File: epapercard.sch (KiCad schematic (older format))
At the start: 43 parts, among them P1 CONN_01X06, P2 A120699CT, Q1 2N7002KW, Q2 BSS84W, Q3 AP2305, Q4 BSS84W, Q5 2N7002KW, Q6 2N7002KW, Q7 2N7002KW, SW1 SW_PUSH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

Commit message: Generated BOM
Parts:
- C2: value 100n -> 0.1u
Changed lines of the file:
@@
 P 3500 5500
 F 0 "C2" H 3525 5600 50  0000 L CNN
-F 1 "100n" H 3525 5400 50  0000 L CNN
+F 1 "0.1u" H 3525 5400 50  0000 L CNN
 F 2 "Capacitors_SMD:C_0805_HandSoldering" H 3538 5350 50  0001 C CNN
 F 3 "" H 3500 5500 50  0000 C CNN

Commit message: Changed fet position
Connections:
- net +3V3: now also Q2.2 (S); no longer Q2.3 (D)
- net at C1.2, Q3.1 (G), R1.1: now also Q2.3 (D); no longer Q2.2 (S)
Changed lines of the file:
@@
 $EndComp
 Wire Wire Line
-	1550 700  1550 1300
+	1550 700  1550 800
+Wire Wire Line
+	1550 800  1550 1300
 Wire Wire Line
 	1550 1300 1700 1300
@@
 	8100 4400 9150 4400
 Wire Wire Line
-	9150 4350 9150 4450
+	9150 4350 9150 4400
+Wire Wire Line
+	9150 4400 9150 4450
 Wire Wire Line
 	9150 4350 9650 4350
@@
 $EndComp
 Wire Wire Line
-	6150 5250 8900 5250
+	6150 5250 6250 5250
+Wire Wire Line
+	6250 5250 8900 5250
 Wire Wire Line
 	8900 4950 9650 4950
@@
 	6250 5450 5800 5450
 Wire Wire Line
-	5800 5450 5800 6000
+	5800 5450 5800 5600
+Wire Wire Line
+	5800 5600 5800 6000
 Wire Wire Line
 	5800 5600 6150 5600
@@
 $EndComp
 Wire Wire Line
-	6350 5900 6350 6050
+	6350 5900 6350 6000
+Wire Wire Line
+	6350 6000 6350 6050
 Wire Wire Line
 	6350 6000 6200 6000
@@
 	9500 5600 8250 5600
 Wire Wire Line
-	9500 5150 9500 5600
+	9500 5150 9500 5250
+Wire Wire Line
+	9500 5250 9500 5600
 Wire Wire Line
 	9500 5250 9650 5250
@@
 F 3 "" H 2300 3000 50  0000 C CNN
 	1    2300 3000
-	1    0    0    -1
+	1    0    0    1
 $EndComp
 $Comp
@@
 $EndComp
 Wire Wire Line
-	1350 3600 1550 3600
+	1350 3600 1450 3600
+Wire Wire Line
+	1450 3600 1550 3600
 Text GLabel 1350 3600 0    60   Input ~ 0
 PANEL_ON
@@
 	2550 3300 2400 3300
 Wire Wire Line
-	2400 3300 2400 3200
+	2400 3300 2400 3250
+Wire Wire Line
+	2400 3250 2400 3200
 $Comp
 L R R1
@@
 	1850 3250 1950 3250
 Wire Wire Line
-	2250 3250 3550 3250
+	2250 3250 2400 3250
+Wire Wire Line
+	2400 3250 3550 3250
 Connection ~ 2400 3250
 $Comp
@@
 	2550 3750 2550 3650
 Wire Wire Line
-	2400 2700 2400 2800
+	2400 2700 2400 2750
+Wire Wire Line
+	2400 2750 2400 2800
 Wire Wire Line
 	3350 2900 2700 2900
@@
 $EndComp
 Wire Wire Line
-	3750 2900 4900 2900
+	3750 2900 4000 2900
+Wire Wire Line
+	4000 2900 4450 2900
+Wire Wire Line
+	4450 2900 4900 2900
 Wire Wire Line
 	4000 2900 4000 2950
@@
 DISCHARGE
 Wire Wire Line
-	5750 4550 6100 4550
+	5750 4550 5900 4550
+Wire Wire Line
+	5900 4550 6100 4550
 Connection ~ 5900 4550
 Wire Wire Line
@@
 	6100 1500 6100 1550
 Wire Wire Line
-	6100 1550 6650 1550
+	6100 1550 6350 1550
+Wire Wire Line
+	6350 1550 6650 1550
 Wire Wire Line
 	6350 1550 6350 1600
@@
 	6100 1200 6100 1150
 Wire Wire Line
-	6100 1150 6650 1150
+	6100 1150 6350 1150
+Wire Wire Line
+	6350 1150 6650 1150
 Wire Wire Line
 	6350 1150 6350 1100

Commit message: Adjusting footprints
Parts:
- Q3: value AP2305 -> BSS84W
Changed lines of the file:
@@
 	4200 900  5450 900
-Wire Wire Line
-	9650 1350 9250 1350
-Wire Wire Line
-	9650 1450 9250 1450
-Wire Wire Line
-	9650 1550 9500 1550
-Wire Wire Line
-	9650 1650 9250 1650
-Wire Wire Line
-	9650 1750 9250 1750
-Wire Wire Line
-	9250 1850 9650 1850
-Wire Wire Line
-	9650 1950 9250 1950
 Wire Wire Line
 	8900 2150 9650 2150
@@
 P 3550 3000
 F 0 "Q3" H 3850 3050 50  0000 R CNN
-F 1 "AP2305" H 4050 2950 50  0000 R CNN
+F 1 "BSS84W" H 4050 2950 50  0000 R CNN
 F 2 "TO_SOT_Packages_SMD:SOT-323" H 3750 3100 50  0001 C CNN
 F 3 "" H 3550 3000 50  0000 C CNN
@@
 	1250 1100 1250 1150
 NoConn ~ 4200 1500
+Wire Wire Line
+	9650 1950 9250 1950
+Wire Wire Line
+	9250 1850 9650 1850
+Wire Wire Line
+	9650 1750 9250 1750
+Wire Wire Line
+	9650 1650 9250 1650
+Wire Wire Line
+	9650 1550 9500 1550
+Wire Wire Line
+	9650 1450 9250 1450
+Wire Wire Line
+	9650 1350 9250 1350
 $EndSCHEMATC

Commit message: Routed caps
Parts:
- U1: footprint Housings_SSOP:TSSOP-20_4.4x6.5mm_Pitch0.65mm -> footprint:TSSOP-20_4.4x6.5mm_Pitch0.65mm
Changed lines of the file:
@@
 F 0 "U1" H 2950 1650 50  0000 C CNN
 F 1 "MSP430G2553IPW20R" H 2950 1850 50  0000 C CNN
-F 2 "Housings_SSOP:TSSOP-20_4.4x6.5mm_Pitch0.65mm" H 2950 1750 50  0001 C CNN
+F 2 "footprint:TSSOP-20_4.4x6.5mm_Pitch0.65mm" H 2950 1750 50  0001 C CNN
 F 3 "DOCUMENTATION" H 2950 1750 50  0001 C CNN
 	1    2950 1750
@@
 $EndComp
 Wire Wire Line
-	1550 700  1550 800
-Wire Wire Line
-	1550 800  1550 1300
+	1550 700  1550 1300
 Wire Wire Line
 	1550 1300 1700 1300
@@
 	8100 4400 9150 4400
 Wire Wire Line
-	9150 4350 9150 4400
-Wire Wire Line
-	9150 4400 9150 4450
+	9150 4350 9150 4450
 Wire Wire Line
 	9150 4350 9650 4350
@@
 $EndComp
 Wire Wire Line
-	6150 5250 6250 5250
-Wire Wire Line
-	6250 5250 8900 5250
+	6150 5250 8900 5250
 Wire Wire Line
 	8900 4950 9650 4950
@@
 	6250 5450 5800 5450
 Wire Wire Line
-	5800 5450 5800 5600
-Wire Wire Line
-	5800 5600 5800 6000
+	5800 5450 5800 6000
 Wire Wire Line
 	5800 5600 6150 5600
@@
 $EndComp
 Wire Wire Line
-	6350 5900 6350 6000
-Wire Wire Line
-	6350 6000 6350 6050
+	6350 5900 6350 6050
 Wire Wire Line
 	6350 6000 6200 6000
@@
 	9500 5600 8250 5600
 Wire Wire Line
-	9500 5150 9500 5250
-Wire Wire Line
-	9500 5250 9500 5600
+	9500 5150 9500 5600
 Wire Wire Line
 	9500 5250 9650 5250
@@
 $EndComp
 Wire Wire Line
-	1350 3600 1450 3600
-Wire Wire Line
-	1450 3600 1550 3600
+	1350 3600 1550 3600
 Text GLabel 1350 3600 0    60   Input ~ 0
 PANEL_ON
@@
 	2550 3300 2400 3300
 Wire Wire Line
-	2400 3300 2400 3250
-Wire Wire Line
-	2400 3250 2400 3200
+	2400 3300 2400 3200
 $Comp
 L R R1
@@
 	1850 3250 1950 3250
 Wire Wire Line
-	2250 3250 2400 3250
-Wire Wire Line
-	2400 3250 3550 3250
+	2250 3250 3550 3250
 Connection ~ 2400 3250
 $Comp
@@
 	2550 3750 2550 3650
 Wire Wire Line
-	2400 2700 2400 2750
-Wire Wire Line
-	2400 2750 2400 2800
+	2400 2700 2400 2800
 Wire Wire Line
 	3350 2900 2700 2900
@@
 $EndComp
 Wire Wire Line
-	3750 2900 4000 2900
-Wire Wire Line
-	4000 2900 4450 2900
-Wire Wire Line
-	4450 2900 4900 2900
+	3750 2900 4900 2900
 Wire Wire Line
 	4000 2900 4000 2950
@@
 DISCHARGE
 Wire Wire Line
-	5750 4550 5900 4550
-Wire Wire Line
-	5900 4550 6100 4550
+	5750 4550 6100 4550
 Connection ~ 5900 4550
 Wire Wire Line
@@
 	6100 1500 6100 1550
 Wire Wire Line
-	6100 1550 6350 1550
-Wire Wire Line
-	6350 1550 6650 1550
+	6100 1550 6650 1550
 Wire Wire Line
 	6350 1550 6350 1600
@@
 	6100 1200 6100 1150
 Wire Wire Line
-	6100 1150 6350 1150
-Wire Wire Line
-	6350 1150 6650 1150
+	6100 1150 6650 1150
 Wire Wire Line
 	6350 1150 6350 1100

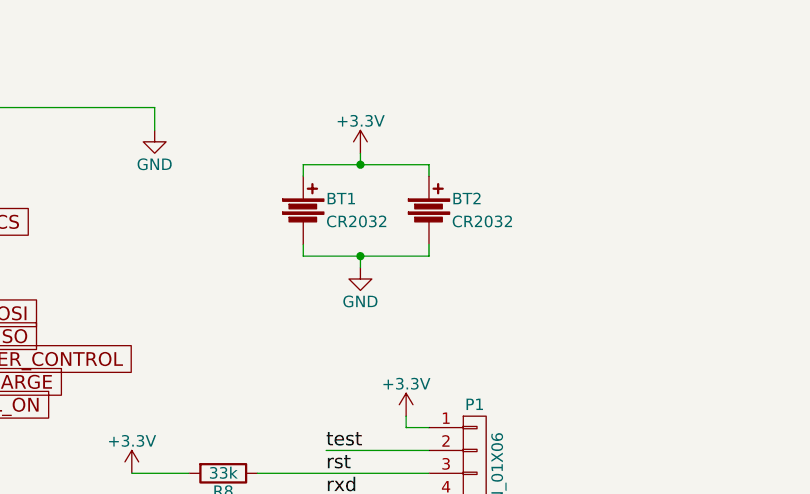
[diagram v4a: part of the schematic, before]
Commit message: Added CR2016 footprint
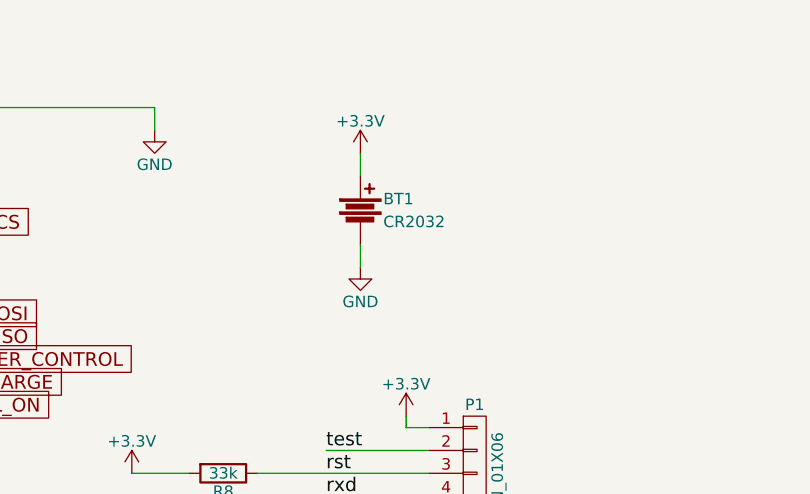
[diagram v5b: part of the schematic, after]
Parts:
- removed BT2: CR2032, footprint:CR2032sm, symbol Battery
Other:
- moved on the sheet: BT1
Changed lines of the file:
@@
 L Battery BT1
 U 1 1 573537BF
-P 6100 1350
-F 0 "BT1" H 6200 1400 50  0000 L CNN
-F 1 "CR2032" H 6200 1300 50  0000 L CNN
-F 2 "footprint:CR2032sm" V 6100 1390 50  0001 C CNN
-F 3 "" V 6100 1390 50  0000 C CNN
-	1    6100 1350
-	1    0    0    -1
-$EndComp
-$Comp
-L Battery BT2
-U 1 1 5735398E
-P 6650 1350
-F 0 "BT2" H 6750 1400 50  0000 L CNN
-F 1 "CR2032" H 6750 1300 50  0000 L CNN
-F 2 "footprint:CR2032sm" V 6650 1390 50  0001 C CNN
-F 3 "" V 6650 1390 50  0000 C CNN
-	1    6650 1350
+P 6350 1350
+F 0 "BT1" H 6450 1400 50  0000 L CNN
+F 1 "CR2032" H 6450 1300 50  0000 L CNN
+F 2 "footprint:CR2032sm" V 6350 1390 50  0001 C CNN
+F 3 "" V 6350 1390 50  0000 C CNN
+	1    6350 1350
 	1    0    0    -1
 $EndComp
@@
 	1    0    0    -1
 $EndComp
-Wire Wire Line
-	6100 1500 6100 1550
-Wire Wire Line
-	6100 1550 6650 1550
-Wire Wire Line
-	6350 1550 6350 1600
-Wire Wire Line
-	6650 1550 6650 1500
-Connection ~ 6350 1550
 $Comp
 L +3.3V #PWR026
@@
 	1    0    0    -1
 $EndComp
-Wire Wire Line
-	6100 1200 6100 1150
-Wire Wire Line
-	6100 1150 6650 1150
-Wire Wire Line
-	6350 1150 6350 1100
-Wire Wire Line
-	6650 1150 6650 1200
-Connection ~ 6350 1150
 $Comp
 L CONN_01X06 P1
@@
 Wire Wire Line
 	9650 1350 9250 1350
+Wire Wire Line
+	6350 1100 6350 1200
+Wire Wire Line
+	6350 1600 6350 1500
 $EndSCHEMATC

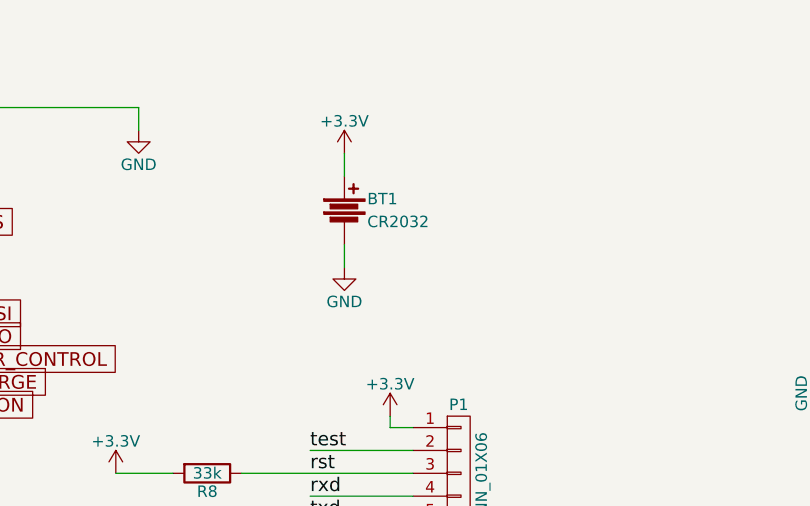
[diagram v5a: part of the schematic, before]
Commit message: Changed battery footprint
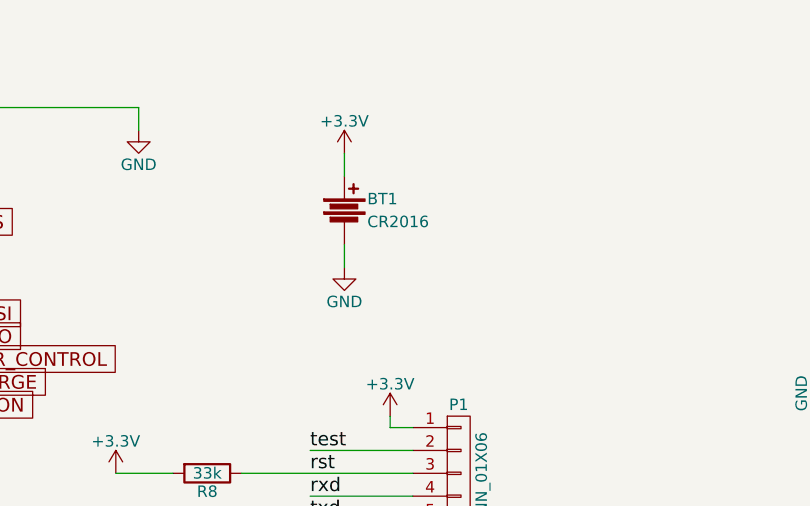
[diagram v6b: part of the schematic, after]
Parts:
- BT1: value CR2032 -> CR2016; footprint footprint:CR2032sm -> footprint:CR2016sm
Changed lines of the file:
@@
 led
-$Comp
-L Battery BT1
-U 1 1 573537BF
-P 6350 1350
-F 0 "BT1" H 6450 1400 50  0000 L CNN
-F 1 "CR2032" H 6450 1300 50  0000 L CNN
-F 2 "footprint:CR2032sm" V 6350 1390 50  0001 C CNN
-F 3 "" V 6350 1390 50  0000 C CNN
-	1    6350 1350
-	1    0    0    -1
-$EndComp
 $Comp
 L GND #PWR025
@@
 Wire Wire Line
 	6350 1600 6350 1500
+$Comp
+L Battery BT1
+U 1 1 573537BF
+P 6350 1350
+F 0 "BT1" H 6450 1400 50  0000 L CNN
+F 1 "CR2016" H 6450 1300 50  0000 L CNN
+F 2 "footprint:CR2016sm" V 6350 1390 50  0001 C CNN
+F 3 "" V 6350 1390 50  0000 C CNN
+	1    6350 1350
+	1    0    0    -1
+$EndComp
 $EndSCHEMATC

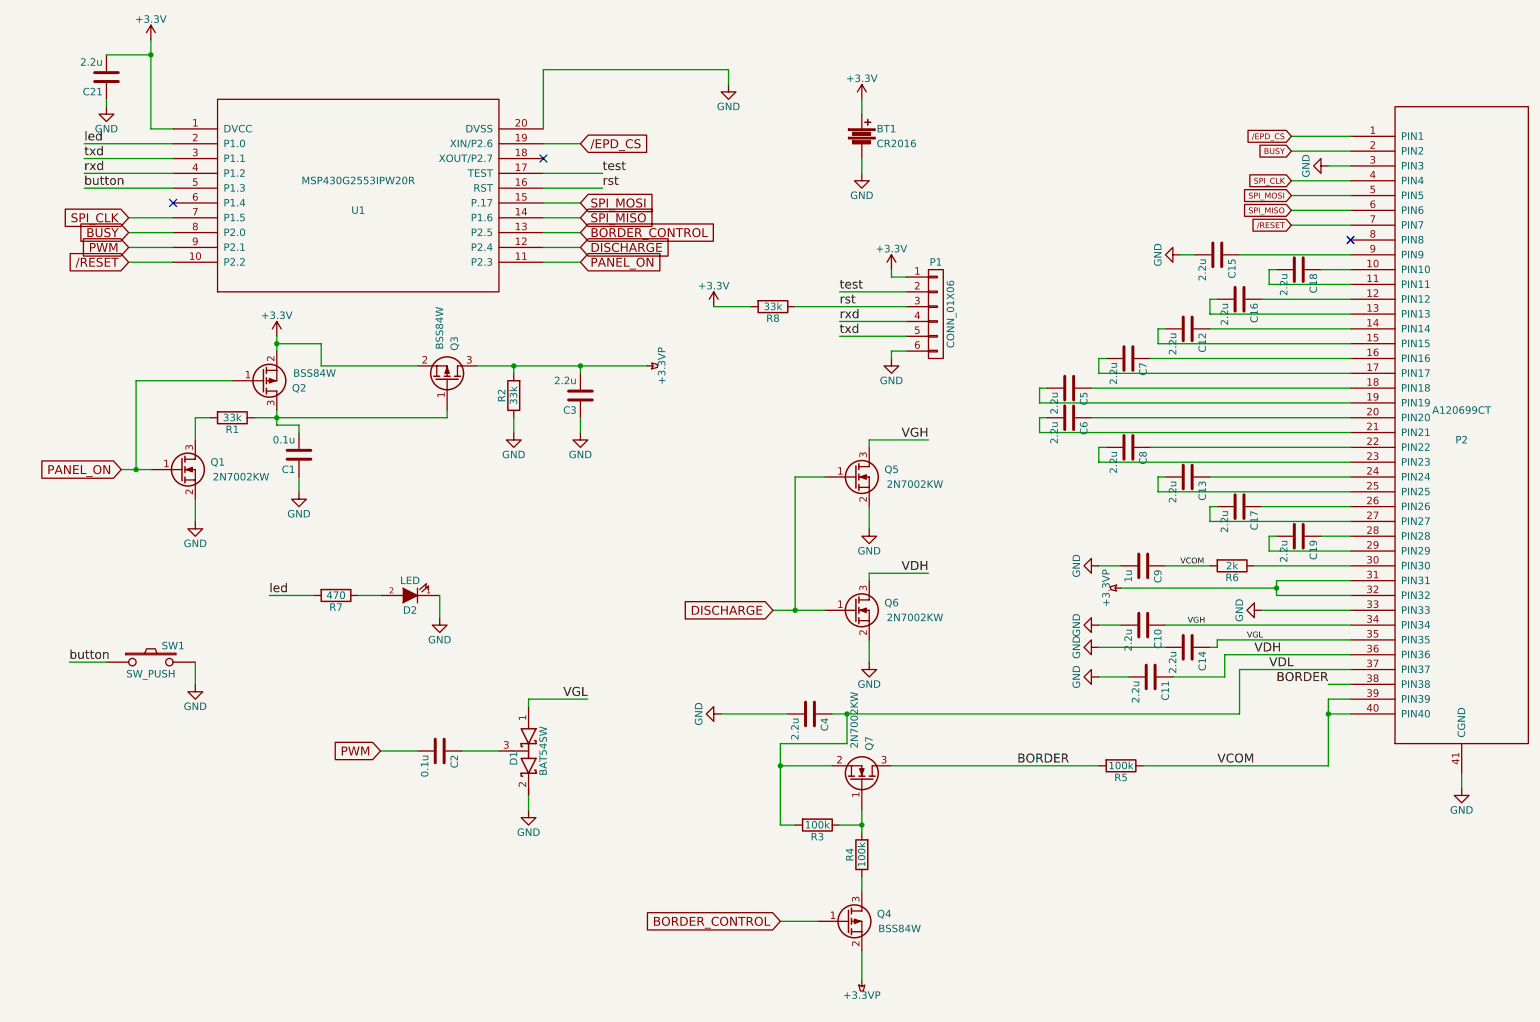
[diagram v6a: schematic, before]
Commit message: Added boost regulator
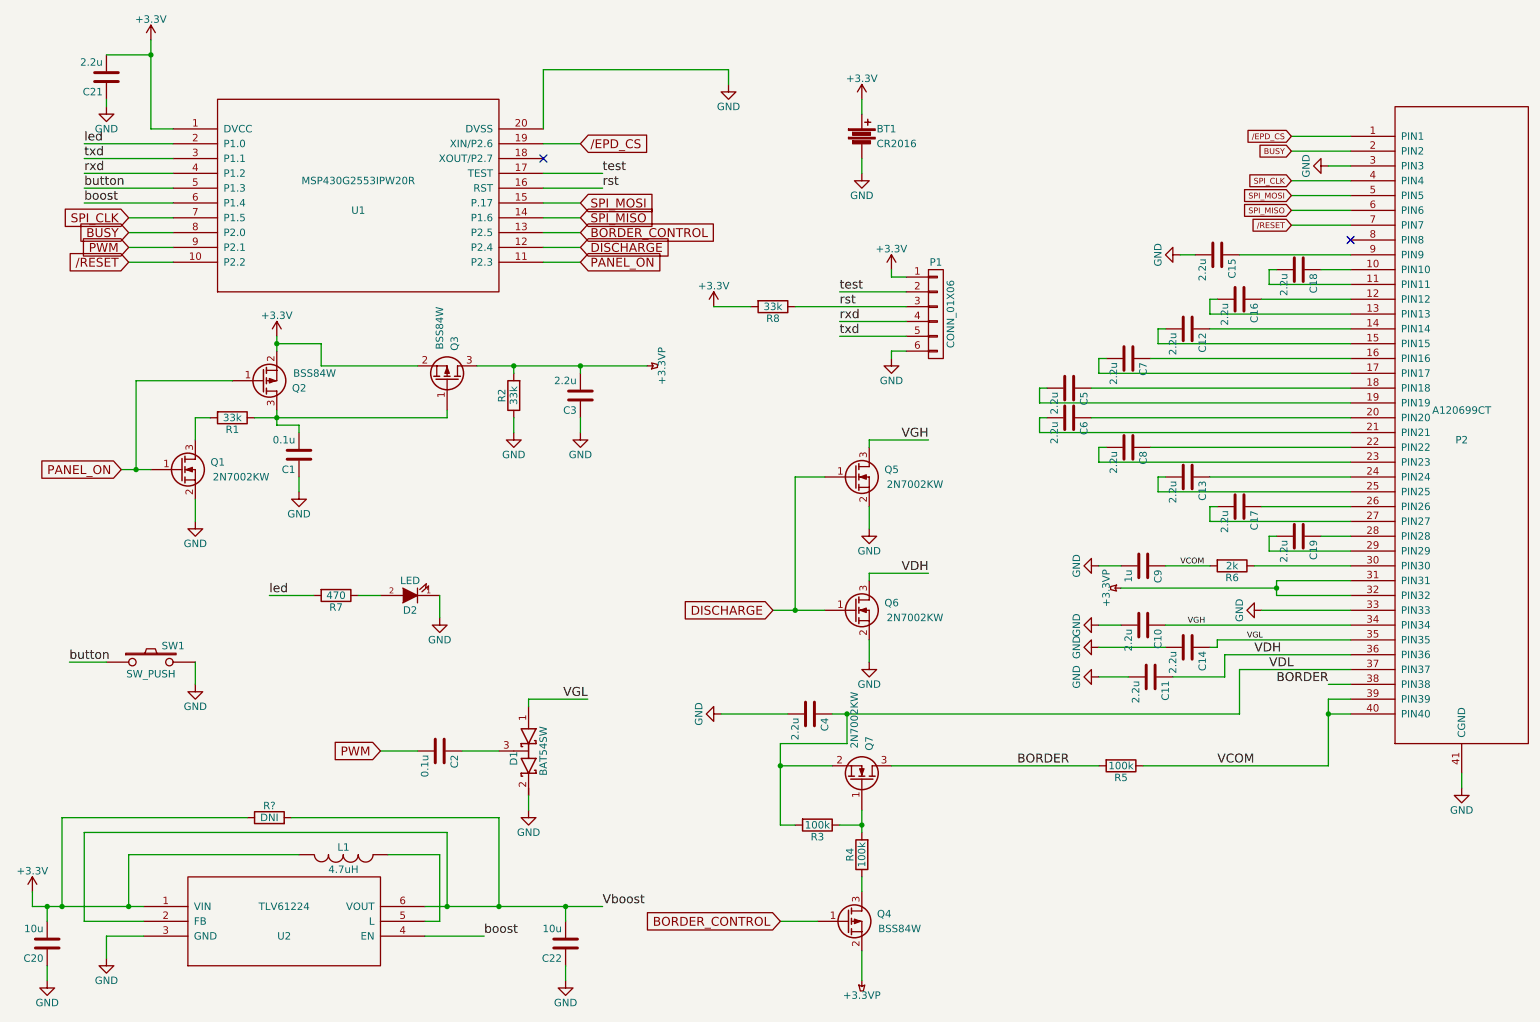
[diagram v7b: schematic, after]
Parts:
- added C20, C22: 10u, Capacitors_SMD:C_0805_HandSoldering, symbol C
- added L1: 4.7uH, Inductors:Inductor_1212, symbol INDUCTOR
- added R?: DNI, Resistors_SMD:R_0201, symbol R
- added U2: TLV61224, TO_SOT_Packages_SMD:SOT-23-6_Handsoldering, symbol TLV61224
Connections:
- net +3V3: now also C20.2, L1.1, R?.1, U2.1 (VIN)
- net GND: now also C20.1, C22.1, U2.3 (GND)
- net boost: now reaches U1.6 (P1.4)
- net boost: now also U2.4 (EN)
- new net: L1.2, U2.5 (L)
- new net Vboost: C22.2, R?.2, U2.2 (FB), U2.6 (VOUT)
- no-connect marks 3 -> 2
